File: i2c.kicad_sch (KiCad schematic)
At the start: 22 parts, among them J20 I2C, J21 RJ45, J23 5V Isolation, J24 GND Isolation, U8 PCA9615DP

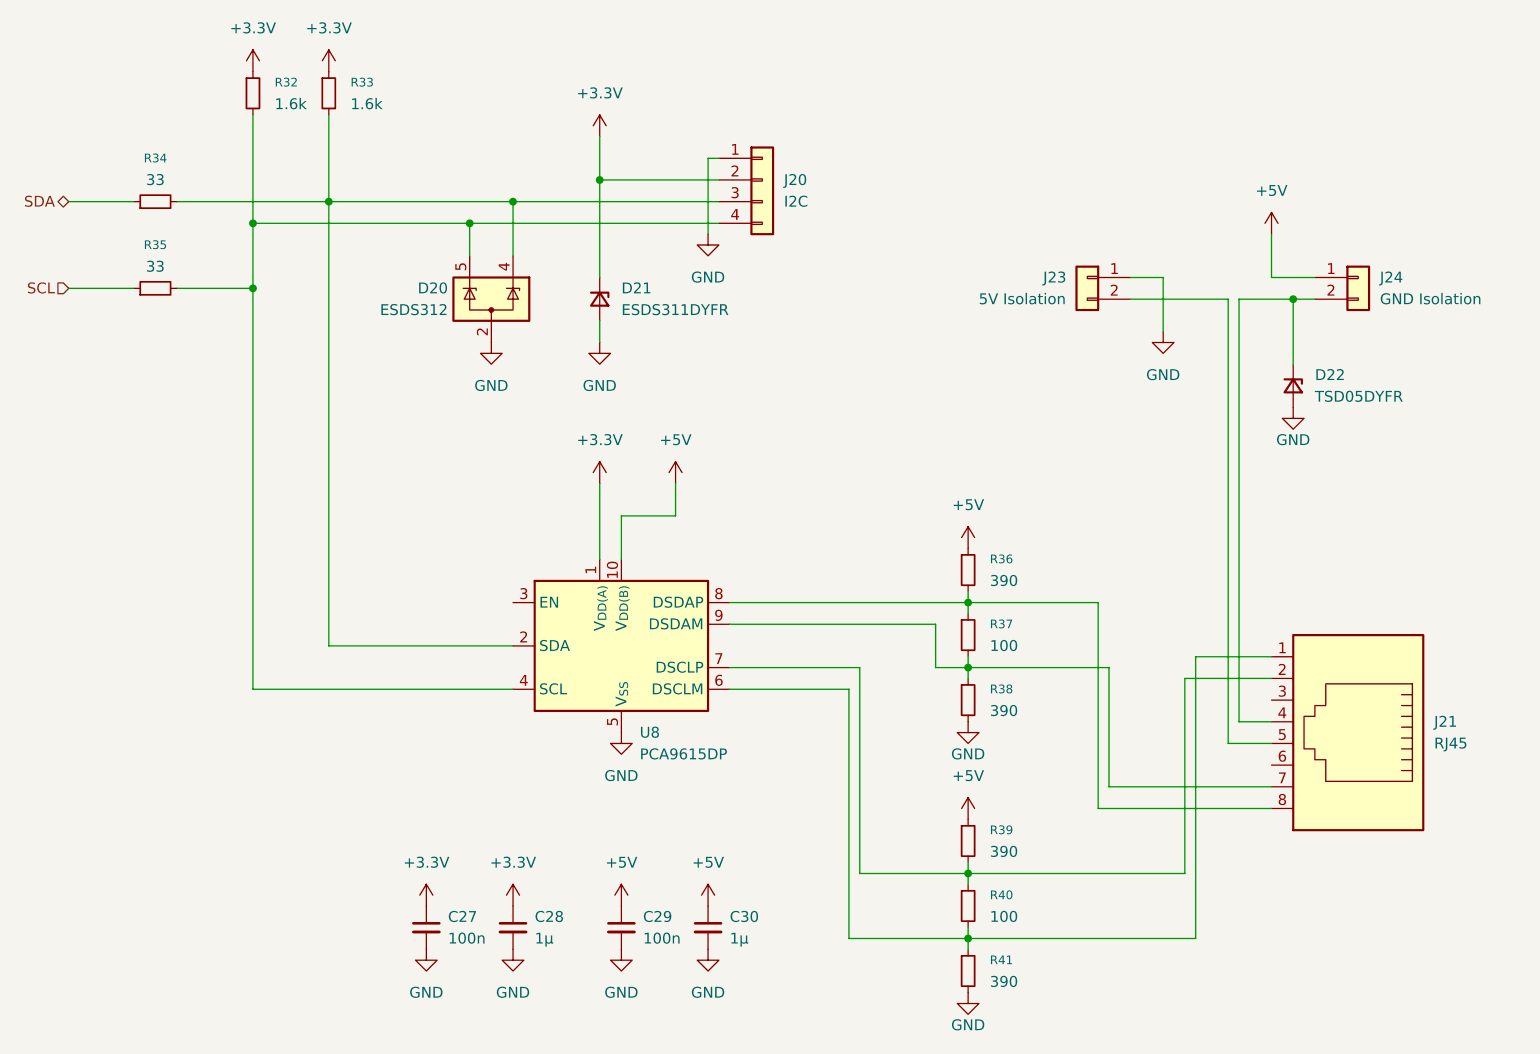
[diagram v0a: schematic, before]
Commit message: - I2C entfernt - Logo hinzugefügt - Spannungsauswahl für Audio (USB oder +5V) hinzugefügt - Spannung für WS2812 LEDs ändert sich jetzt zusammen mit +5VD Auswahl
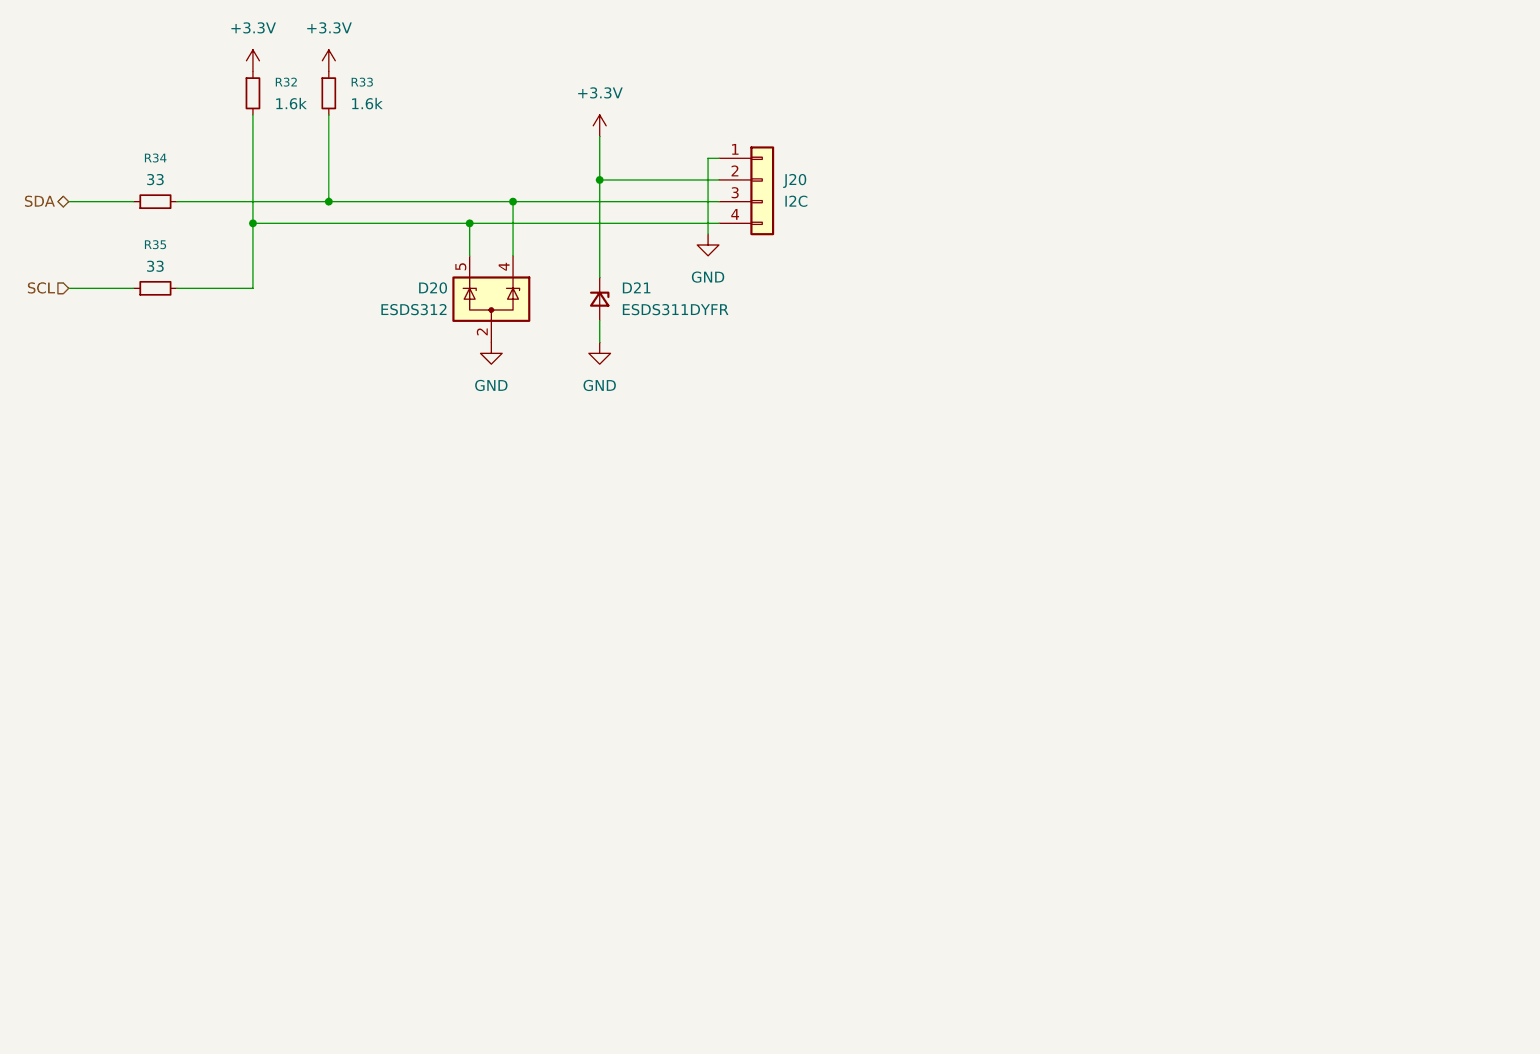
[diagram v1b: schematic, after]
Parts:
- removed C27, C29: 100n, Capacitor_SMD:C_0603_1608Metric, symbol Device:C_Small
- removed C28, C30: 1µ, Capacitor_SMD:C_0603_1608Metric, symbol Device:C_Small
- removed D22: TSD05DYFR, Diode_SMD:D_SOD-323_HandSoldering, symbol Device:D_Zener_Small
- removed J21: RJ45, Connector_RJ:RJ45_Amphenol_54602-x08_Horizontal, symbol Connector:RJ45
- removed J23: 5V Isolation, Connector_PinHeader_2.54mm:PinHeader_1x02_P2.54mm_Vertical, symbol Connector_Generic:Conn_01x02
- removed J24: GND Isolation, Connector_PinHeader_2.54mm:PinHeader_1x02_P2.54mm_Vertical, symbol Connector_Generic:Conn_01x02
- removed R36, R38, R39, R41: 390, Resistor_SMD:R_0603_1608Metric, symbol Device:R_Small
- removed R37, R40: 100, Resistor_SMD:R_0603_1608Metric, symbol Device:R_Small
- removed U8: PCA9615DP, Package_SO:TSSOP-10_3x3mm_P0.5mm, symbol Interface:PCA9615DP
